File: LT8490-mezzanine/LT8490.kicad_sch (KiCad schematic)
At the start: 122 parts, among them J1 Conn_01x01, J10 Conn_01x01, J11 Conn_01x01, J12 Conn_01x01, J13 Conn_01x01, J14 Conn_01x01, J15 Conn_01x01, J16 Conn_01x01, J17 Conn_01x01, J18 Conn_01x01, J19 Conn_01x01, J2 Conn_01x01, J20 Conn_01x01, J21 Conn_01x01, J22 Conn_01x01, J23 Conn_01x01, J24 Conn_01x01, J25 Conn_01x01, J3 Conn_01x01, J4 Conn_01x01, J5 Conn_01x01, J6 Conn_01x01, J7 Conn_01x01, J8 Conn_01x01, J9 Conn_01x01, Q1 Si7106DN, Q2 Si7106DN, Q3 Si7106DN, Q4 Si7106DN, Q5 BSS84, Q6 MBT2222ADW1T1, U4 LT8490EUKJPBF

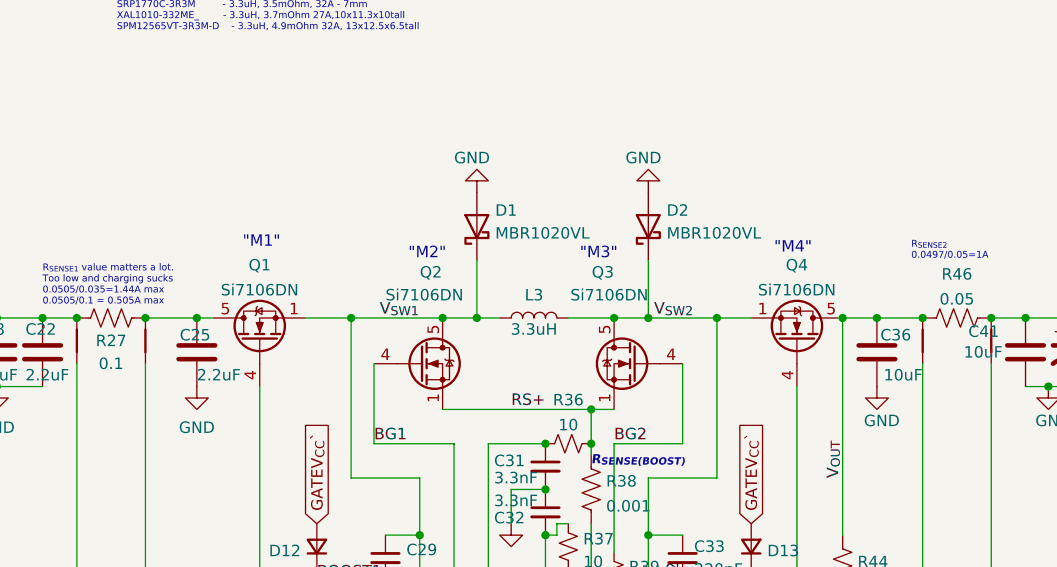
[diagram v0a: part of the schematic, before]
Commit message: changed components to allow 23V input
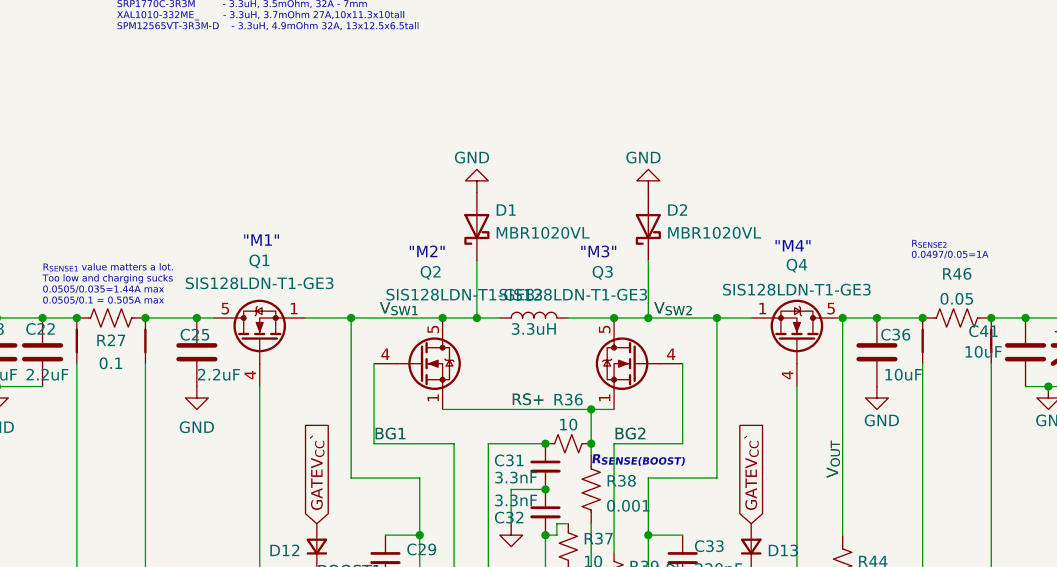
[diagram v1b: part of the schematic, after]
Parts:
- Q1, Q2, Q3, Q4: value Si7106DN -> SIS128LDN-T1-GE3; Manufacturer_Part_Number Si7106DN -> SIS128LDN-T1-GE3

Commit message: made component changes to allow 23V input
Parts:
- C17: footprint Capacitor_SMD:C_0603_1608Metric -> Capacitor_SMD:C_0805_2012Metric
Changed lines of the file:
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@@
       (effects (font (size 1.27 1.27)) (justify right))
     )
-    (property "Footprint" "Capacitor_SMD:C_0603_1608Metric" (at 54.61 102.87 0)
+    (property "Footprint" "Capacitor_SMD:C_0805_2012Metric" (at 54.61 102.87 0)
       (effects (font (size 1.27 1.27)) hide)
     )
@@
       (effects (font (size 1.27 1.27)) hide)
     )
-    (property "Description" "2.2uF 0603" (at 52.2859 112.1278 0)
+    (property "Description" "2.2uF 0803" (at 52.2859 112.1278 0)
       (effects (font (size 1.27 1.27)) (justify right) hide)
     )

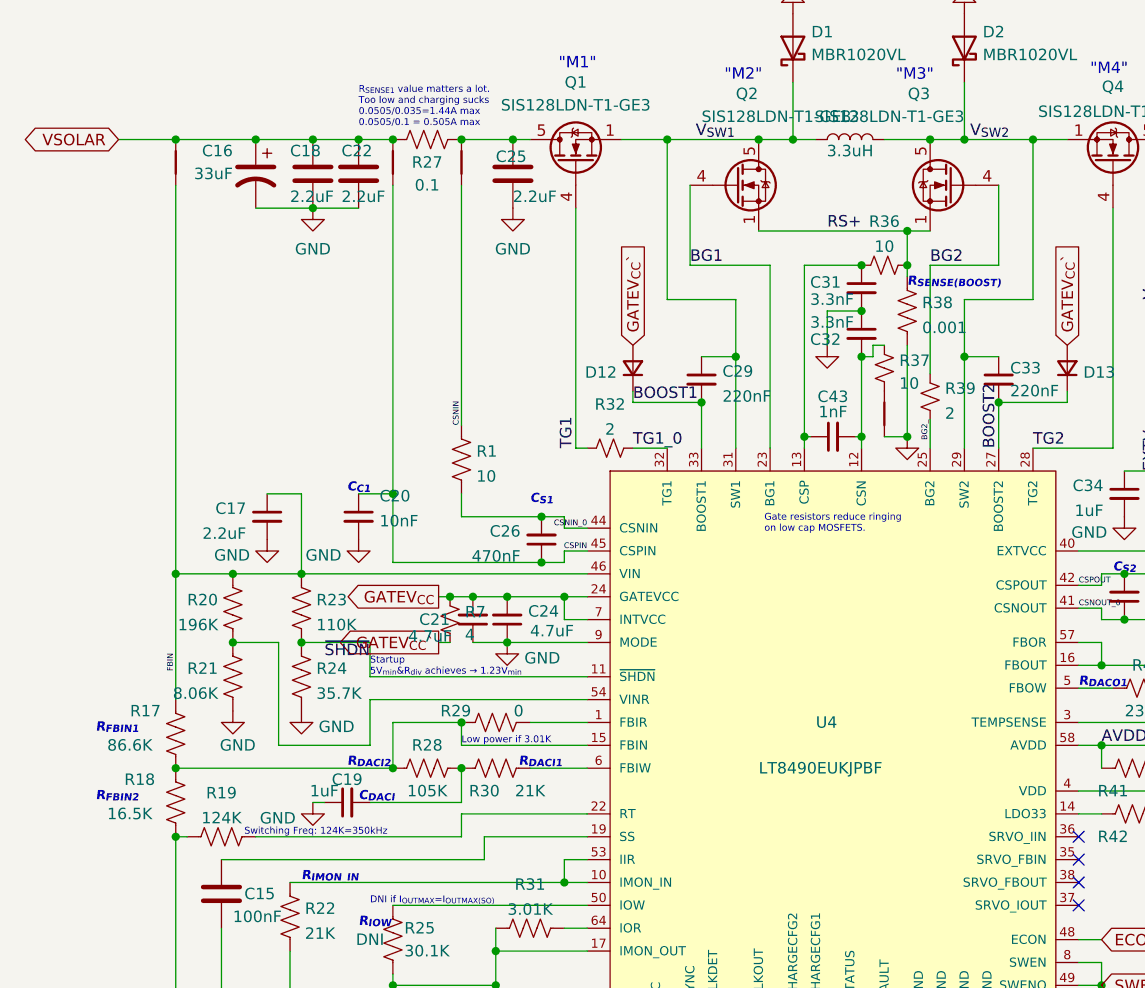
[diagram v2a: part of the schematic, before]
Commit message: actaully changed values to reflect 23V input
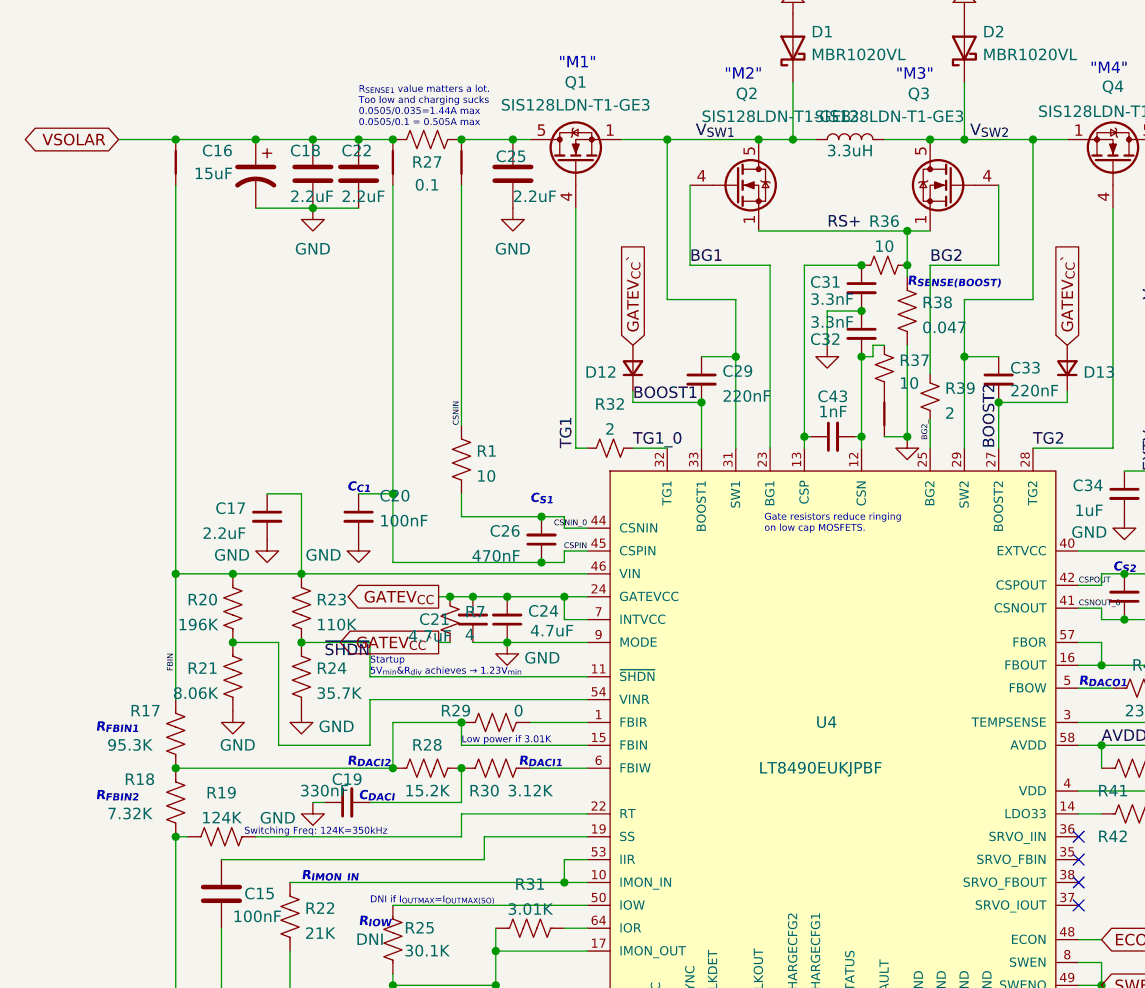
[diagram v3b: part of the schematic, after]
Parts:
- C16: value 33uF -> 15uF; Voltage 16V -> 75V
- C19: value 1uF -> 330nF
- C20: value 10nF -> 100nF
- R17: value 86.6K -> 95.3K
- R18: value 16.5K -> 7.32K
- R28: value 105K -> 15.2K
- R30: value 21K -> 3.12K
- R38: value 0.001 -> 0.047
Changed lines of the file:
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@@
       (effects (font (size 1.27 1.27)))
     )
-    (property "Value" "105K" (at 72.39 133.35 90)
+    (property "Value" "15.2K" (at 72.39 133.35 90)
       (effects (font (size 1.27 1.27)))
     )
@@
       (effects (font (size 1.27 1.27)) hide)
     )
-    (property "Description" "105K 0603" (at 72.39 138.43 90)
+    (property "Description" "15.2K 0603" (at 72.39 138.43 90)
       (effects (font (size 1.27 1.27)) hide)
     )
@@
       (effects (font (size 1.27 1.27)) (justify left))
     )
-    (property "Value" "16.5K" (at 36.83 135.89 0)
+    (property "Value" "7.32K" (at 36.83 135.89 0)
       (effects (font (size 1.27 1.27)) (justify left))
     )
@@
       (effects (font (size 1.27 1.27)) hide)
     )
-    (property "Description" "16.5K 0603" (at 38.735 142.24 0)
+    (property "Description" "7.32K 0603" (at 38.735 142.24 0)
       (effects (font (size 1.27 1.27)) (justify left) hide)
     )
@@
       (effects (font (size 1.27 1.27)))
     )
-    (property "Value" "1uF" (at 60.96 133.35 90)
+    (property "Value" "330nF" (at 60.96 133.35 90)
       (effects (font (size 1.27 1.27)))
     )
@@
       (effects (font (size 1.27 1.27)) hide)
     )
-    (property "Description" "1uF 0603" (at 63.5 142.24 90)
+    (property "Description" "330nF 0603" (at 63.5 142.24 90)
       (effects (font (size 1.27 1.27)) hide)
     )
@@
       (effects (font (size 1.27 1.27)) (justify left))
     )
-    (property "Value" "33uF" (at 50.8 64.77 0)
+    (property "Value" "15uF" (at 50.8 64.77 0)
       (effects (font (size 1.27 1.27)) (justify left))
     )
@@
       (effects (font (size 1.27 1.27)) hide)
     )
-    (property "Voltage" "16V" (at 50.8 67.31 0)
+    (property "Voltage" "75V" (at 50.8 67.31 0)
       (effects (font (size 1.27 1.27)) (justify left) hide)
     )
@@
       (effects (font (size 1.27 1.27)) (justify left))
     )
-    (property "Value" "86.6K" (at 36.83 128.27 0)
+    (property "Value" "95.3K" (at 36.83 128.27 0)
       (effects (font (size 1.27 1.27)) (justify left))
     )
@@
       (effects (font (size 1.27 1.27)) hide)
     )
-    (property "Description" "86.6K 0603" (at 39.37 134.62 0)
+    (property "Description" "95.3K 0603" (at 39.37 134.62 0)
       (effects (font (size 1.27 1.27)) (justify left) hide)
     )
@@
       (effects (font (size 1.27 1.27)) (justify left))
     )
-    (property "Value" "10nF" (at 67.0941 103.3553 0)
+    (property "Value" "100nF" (at 67.0941 103.3553 0)
       (effects (font (size 1.27 1.27)) (justify left))
     )
@@
       (effects (font (size 1.27 1.27)) hide)
     )
-    (property "Description" "10nF 0603" (at 67.0941 113.2802 0)
+    (property "Description" "100nF 0603" (at 67.0941 113.2802 0)
       (effects (font (size 1.27 1.27)) (justify left) hide)
     )
@@
       (effects (font (size 1.27 1.27)))
     )
-    (property "Value" "21K" (at 83.82 133.35 90)
+    (property "Value" "3.12K" (at 83.82 133.35 90)
       (effects (font (size 1.27 1.27)))
     )
@@
       (effects (font (size 1.27 1.27)) hide)
     )
-    (property "Description" "21K 0603" (at 78.74 143.51 90)
+    (property "Description" "3.12K 0603" (at 78.74 143.51 90)
       (effects (font (size 1.27 1.27)) hide)
     )
@@
       (effects (font (size 1.27 1.27)) (justify left))
     )
-    (property "Value" "0.001" (at 127.381 81.8766 0)
+    (property "Value" "0.047" (at 127.381 81.8766 0)
       (effects (font (size 1.27 1.27)) (justify left))
     )
@@
       (effects (font (size 1.27 1.27)) hide)
     )
-    (property "Description" "0.001 1206" (at 127.381 89.2615 0)
-      (effects (font (size 1.27 1.27)) (justify left) hide)
-    )
+    (property "Description" "0.047 1206" (at 127.381 89.2615 0)
+      (effects (font (size 1.27 1.27)) (justify left) hide)
+    )

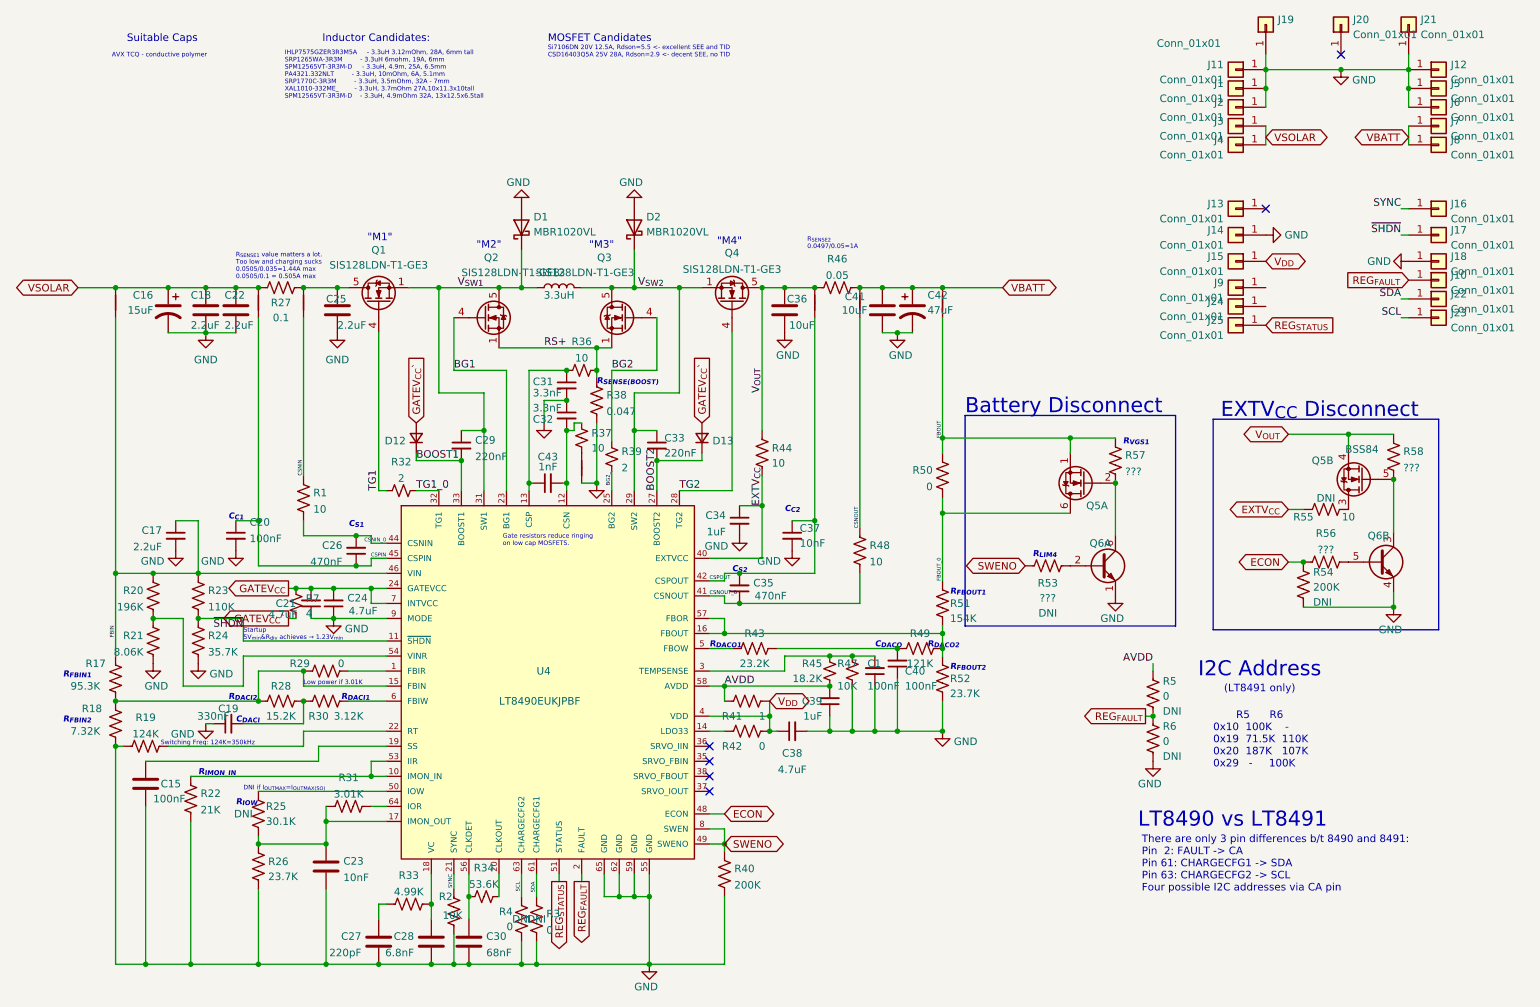
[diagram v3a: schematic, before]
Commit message: v1.0b: edited component values, updated for Kicad 7
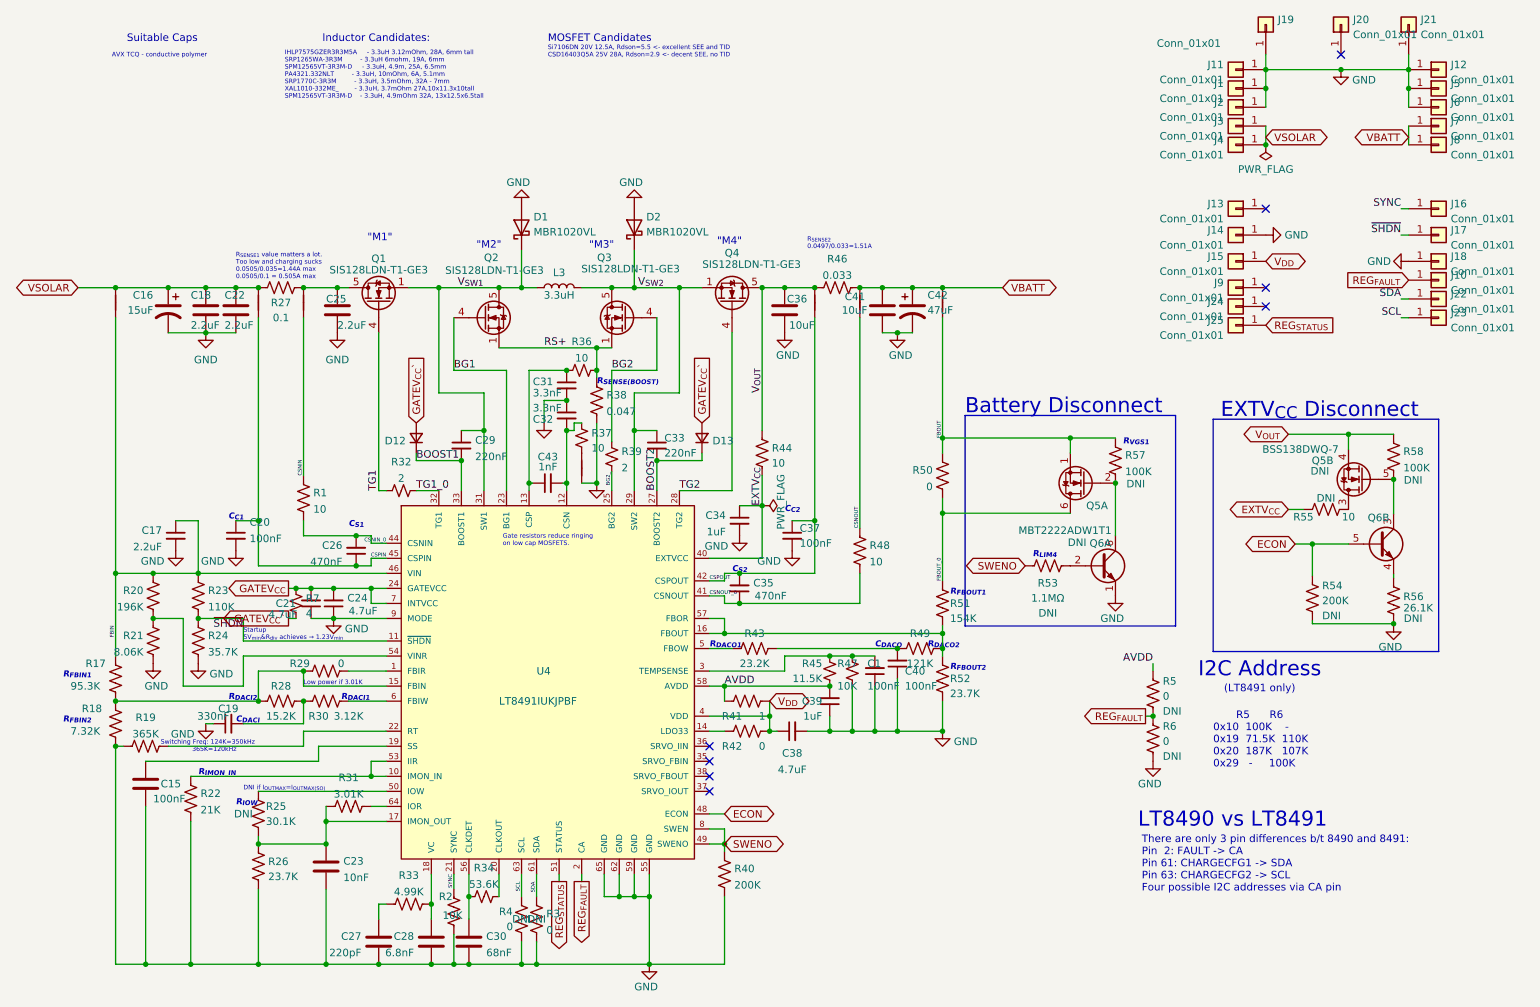
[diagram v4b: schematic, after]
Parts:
- C37: value 10nF -> 100nF
- J1, J10, J11, J12, J13, J14, J15, J16, J17, J18, J19, J2, J20, J21, J22, J23, J24, J25, J3, J4, J5, J6, J7, J8, J9: footprint custom-footprints:castellated_05mm -> mppt:mppt_castellation_05mm; symbol Connector_Generic:Conn_01x01 -> mppt:mppt_castellation_05mm
- L3: footprint custom-footprints:L_SRP1770C -> mppt:L_SRP1770C
- NT1, NT2, NT3, NT4, NT5, NT6, NT7, Q6, R25, R3, R4, R5, R6: now left out of the parts list
- Q1, Q2, Q3, Q4: footprint custom-footprints:SIS862DNT1GE3 -> mppt:SIS128LDN-T1-GE3; symbol Transistor_FET:Si7336ADP -> mppt:SIS128LDN-T1-GE3
- Q5: value BSS84 -> BSS138DWQ-7; footprint custom-footprints:BSS138DWQ-7 -> mainboard:BSS138DWQ-7; symbol ypanel-rescue:BSS138DWQ-7-symbols -> mainboard:BSS138DWQ-7; Height (none) -> 1.1; Manufacturer_Part_Number (none) -> BSS138DWQ-7; Mouser Part Number (none) -> 621-BSS138DWQ-7; Mouser Price/Stock (none) -> https://www.mouser.co.uk/ProductDetail/Diodes-Incorporated/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; now left out of the parts list
- R19: value 124K -> 365K
- R45: value 18.2K -> 11.5K
- R46: value 0.05 -> 0.033
- R53: value ??? -> 1.1MΩ; now left out of the parts list
- R56: value ??? -> 26.1K; now left out of the parts list
- R57, R58: value ??? -> 100K; now left out of the parts list
- U4: value LT8490EUKJPBF -> LT8491IUKJPBF; footprint custom-footprints:LT8490EUKJ#PBF -> mppt:LT8491IUKJ#PBF; symbol symbols:LT8490EUKJPBF -> mppt:LT8491IUKJPBF
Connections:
- net ECON: now also Q6.5 (B2); no longer R56.1
- net GND: now also R56.1; no longer Q6.4 (E2)
- net at R56.2: now also Q6.4 (E2); no longer Q6.5 (B2)
- no-connect marks 6 -> 8
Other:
- note added: "R_{SENSE2} 0.0497/0.033=1.51A"
- note added: "Switching Freq: 124K=350kHz 365K=120kHz"
- note removed: "R_{SENSE2} 0.0497/0.05=1A"
- note removed: "Switching Freq: 124K=350kHz"
- title: (none) -> LT8491 - Mezzanine
- moved on the sheet: Q6B, R54, R56
